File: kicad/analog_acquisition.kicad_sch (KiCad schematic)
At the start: 65 parts, among them J2 BNC_Isolated, J3 BNC_Isolated, J4 JST-XH 3-pin, J5 BNC_Isolated, J6 JST-XH 2-pin, J7 JST-XH 3-pin, T1 Transformer_SP_2S, T2 Transformer_SP_2S, T3 Transformer_SP_2S, U10 MCP6002, U11 MCP6002, U12 SN6501, U13 AMC1301, U4 MCP6002, U5 SN6501, U6 AMC1301, U7 MCP6002, U8 SN6501, U9 AMC1301

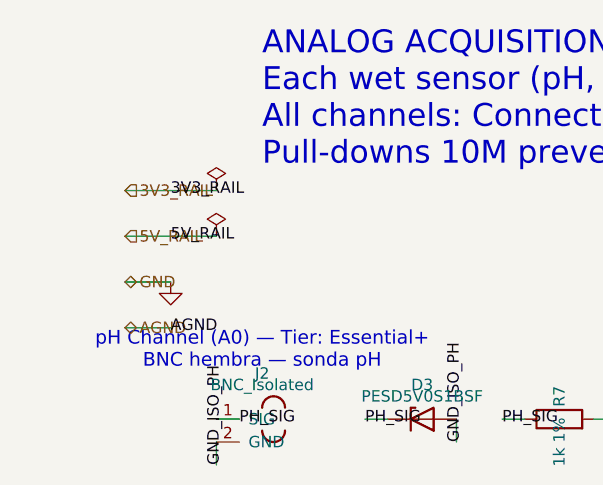
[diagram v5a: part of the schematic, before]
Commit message: fix(erc): clean remaining ERC violations in hierarchical schematics
- Reconnect 5V_RAIL and 3V3_RAIL hierarchical labels in power_management.
- Move MCU_WDI hierarchical label to U3 WDI and add R3 pull-up wiring.
- Add PWR_FLAG sources for GND (power_management) and PGND (actuator_drivers).
- Add 5V_RAIL PWR_FLAG in power_management.
- Remove redundant PWR_FLAGS #FLG40 and #FLG41 from analog_acquisition.
- Place no_connect markers on unused MAX485 U15 left-side pins.
- Change HX711 AVDD pin type from power_out to power_in (library and digital sheet).
- Change Arduino shield header 5V/3V3 pins from power_out to passive.
- Achieve zero ERC violations in kicad-cli sch erc.

Co-Authored-By: Devin AI <158243242+devin-ai-integration[bot]@users.noreply.github.com>
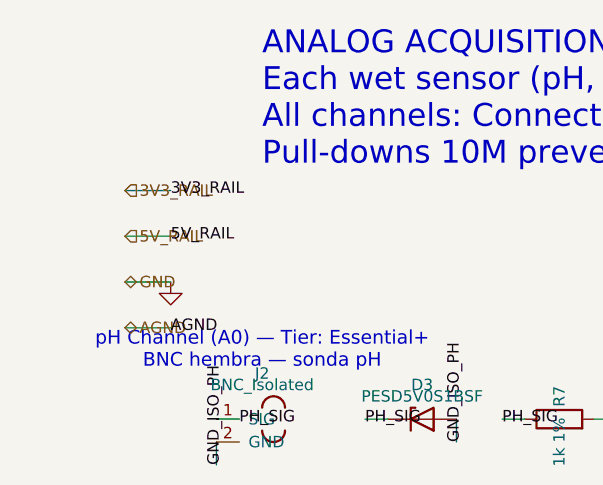
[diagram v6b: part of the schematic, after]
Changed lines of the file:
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@@
     (effects (font (size 1.27 1.27)))
-  )
-  (symbol
-    (lib_id "power:PWR_FLAG")
-    (at 20.32 25.4 0)
-    (unit 1)
-    (exclude_from_sim no) (in_bom no) (on_board no)
-    (property "Reference" "#FLG40" (at 20.32 22.86 0)
-      (effects (font (size 1.27 1.27)) hide))
-    (property "Value" "PWR_FLAG" (at 20.32 24.13 0)
-      (effects (font (size 1.27 1.27)) hide))
-    (pin "1")
-    (instances (project "nebula_qshield"
-      (path "/c6da75fc-541f-4933-b134-f5eb8982a11b/9688e820-0346-4732-9e7d-cc0365bc1e8b" (reference "#FLG40") (unit 1))))
-  )
-  (wire (pts (xy 15.24 25.4) (xy 20.32 25.4))
-    (stroke (width 0) (type default))
   )
   (wire (pts (xy 10.16 30.48) (xy 15.24 30.48))
@@
     (effects (font (size 1.27 1.27)))
   )
-  (symbol
-    (lib_id "power:PWR_FLAG")
-    (at 20.32 30.48 0)
-    (unit 1)
-    (exclude_from_sim no) (in_bom no) (on_board no)
-    (property "Reference" "#FLG41" (at 20.32 27.94 0)
-      (effects (font (size 1.27 1.27)) hide))
-    (property "Value" "PWR_FLAG" (at 20.32 29.21 0)
-      (effects (font (size 1.27 1.27)) hide))
-    (pin "1")
-    (instances (project "nebula_qshield"
-      (path "/c6da75fc-541f-4933-b134-f5eb8982a11b/9688e820-0346-4732-9e7d-cc0365bc1e8b" (reference "#FLG41") (unit 1))))
-  )
-  (wire (pts (xy 15.24 30.48) (xy 20.32 30.48))
-    (stroke (width 0) (type default))
-  )
   (wire (pts (xy 10.16 35.56) (xy 15.24 35.56))

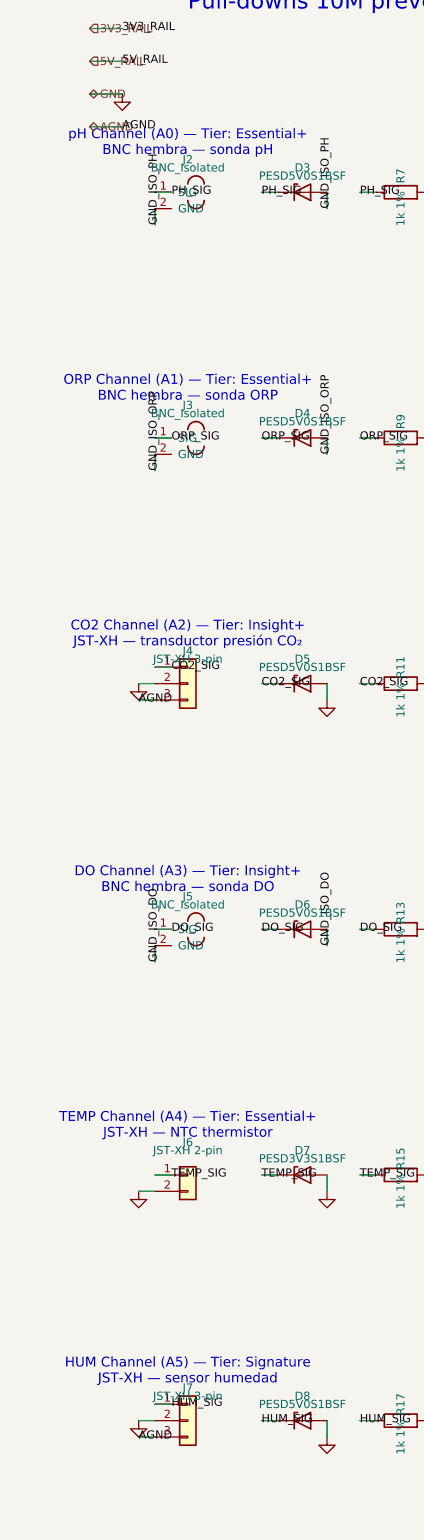
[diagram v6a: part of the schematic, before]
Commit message: fix(grounding): unify AGND/PGND into GND, migrate CI to KiCad 10.0.5 — ERC 14→0
AGND and PGND were fully isolated nets with no path to GND, so the actuator
return path (MOSFET sources, opto emitters, gate-driver COM, flyback diodes,
terminal blocks) and the CO2/humidity sensor returns were floating. Merge them
into the single global GND net per the unified-grounding decision: one
continuous plane on layer 2, star grounding realised through placement and
local vias rather than split nets.

The isolated domains are untouched — GND_ISO_PH/ORP/DO (AMC1301 + SN6501
transformer) and GND_ISO (ISO1541) stay floating, since the galvanic barrier
lives in the isolators, not in a second ground plane.

- analog_acquisition: 2 AGND labels -> GND, legend stub removed
- actuator_drivers: 12 PGND labels -> GND, legend stub and its now-redundant
  PWR_FLAG removed
- hmi_connectors: HMI_TX/HMI_RX demoted from hierarchical to local labels; the
  UART is fully routed inside the sheet and nothing consumed the export
- root: 4 orphan sheet pins with their stub wires and labels removed
- CI container 9.0 -> 10.0.5, ERC severities pinned in the project file so the
  gate cannot weaken through a version bump, threshold 14 -> 0

Netlist verified pin-by-pin: 495 pins before and after, none lost or added,
exactly the 20 intended net reassignments. ERC clean under KiCad 10.0.5.

Co-Authored-By: Devin AI <158243242+devin-ai-integration[bot]@users.noreply.github.com>
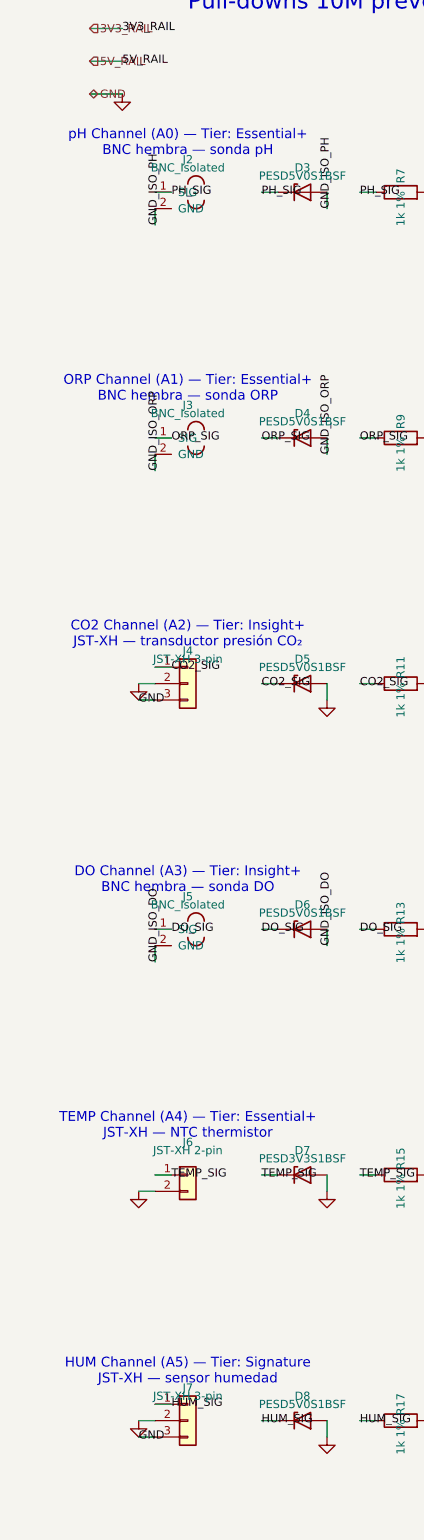
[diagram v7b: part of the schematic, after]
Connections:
- net AGND is gone; now on net GND: J4.3 (Pin_3), J7.3 (Pin_3)
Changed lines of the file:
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@@
   (hierarchical_label "5V_RAIL"  (shape input)  (at 10.16 30.48 0)  (effects (font (size 1.27 1.27))))
   (hierarchical_label "GND"      (shape bidirectional) (at 10.16 35.56 0) (effects (font (size 1.27 1.27))))
-  (hierarchical_label "AGND"     (shape bidirectional) (at 10.16 40.64 0) (effects (font (size 1.27 1.27))))
   (symbol
     (lib_id "Device:C")
@@
       (path "/c6da75fc-541f-4933-b134-f5eb8982a11b/9688e820-0346-4732-9e7d-cc0365bc1e8b" (reference "#PWR020") (unit 1))))
   )
-  (wire (pts (xy 10.16 40.64) (xy 15.24 40.64))
-    (stroke (width 0) (type default))
-  )
-  (label "AGND" (at 15.24 40.64 0)
-    (effects (font (size 1.27 1.27)))
-  )
   (wire (pts (xy 200.66 46.99) (xy 200.66 44.45))
     (stroke (width 0) (type default))
@@
     (stroke (width 0) (type default))
   )
-  (label "AGND" (at 17.78 129.54 0)
+  (label "GND" (at 17.78 129.54 0)
     (effects (font (size 1.27 1.27)))
   )
@@
     (stroke (width 0) (type default))
   )
-  (label "AGND" (at 17.78 243.84 0)
-    (effects (font (size 1.27 1.27)))
-  )
+  (label "GND" (at 17.78 243.84 0)
+    (effects (font (size 1.27 1.27)))
+  )
